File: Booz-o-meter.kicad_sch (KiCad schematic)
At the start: 61 parts, among them J1 Power, J4 Rod, K1 G5V-2, K2 G5V-2, K3 G5V-2, K4 G5V-2, K5 G5V-2, K6 G5V-2, K7 G5V-2, K8 G5V-2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

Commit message: First pass at routing
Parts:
- added H1, H2, H3, H4: MountingHole, MountingHole:MountingHole_3.5mm, symbol Mechanical:MountingHole
- added SW1, SW2: SW_MEC_5E, symbol Switch:SW_MEC_5E
- K1: value G5V-2 -> GAME_ACTIVE1
- K2: value G5V-2 -> GAME_OVER
- K3: value G5V-2 -> ZAPOSC
- K4: value G5V-2 -> GAME_ACTIVE2
- K5: value G5V-2 -> FWD
- K6: value G5V-2 -> LOST
- K7: value G5V-2 -> REV
- K8: value G5V-2 -> WON
- K9: value G5V-2 -> GAME_RESET
- SW_FWD_LIMIT1: symbol Switch:SW_SPDT -> Switch:SW_SPST
- renumbered RV1 to GAME_OVER_TIMER1
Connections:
- net GND: now also SW2.3 (K)
- net VCC: now also K1.1; no longer K1.16
- net game_active: now also K1.16; no longer K1.1
- net at D9.1 (KA), R4.2: now also PB_RESET1.3 (K)
- net at K1.8, K2.13, PB_START1.2: now also SW1.3 (K), SW1.4 (A)
- net at K1.9, K7.1, R10.1: now also D24.1 (K)
- net at D9.2 (AK), K5.13, K7.13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: now also PB_RESET1.4 (A)
- net at PB_START1.1, PB_START1.3 (K), SW_REV_LIMIT1.1 (A): now also SW1.1, SW1.2
- net at D15.1 (K), PB_RESET1.2: now also SW2.2
- no-connect marks 0 -> 3
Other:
- note removed: "**POWER CONNECTOR!!!**"
- note removed: "**VMOTOR**"
- note removed: "**VTRANS**"
- moved on the sheet: D11, D12, R2

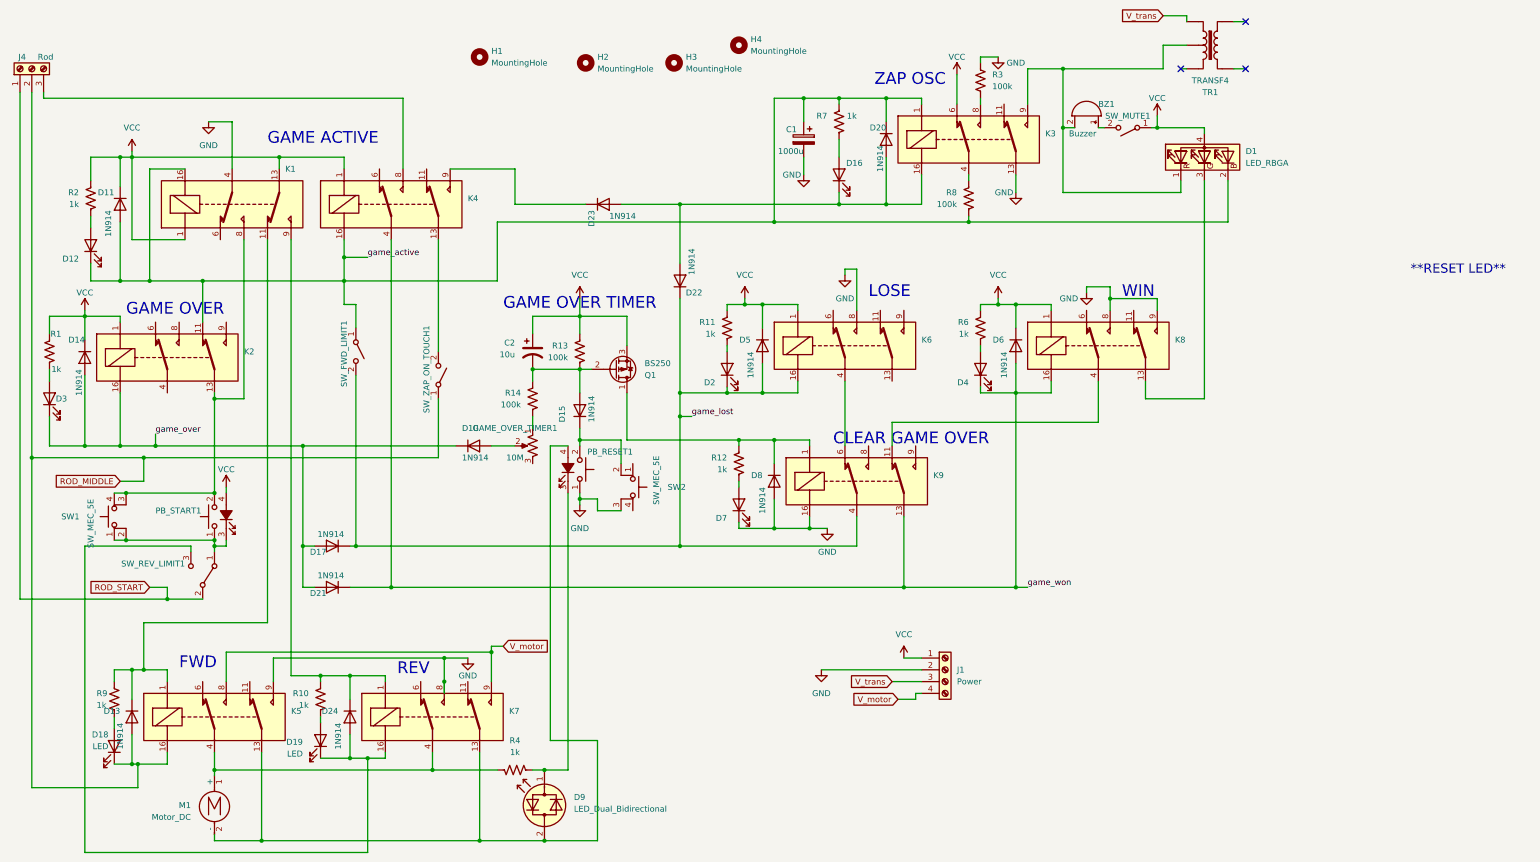
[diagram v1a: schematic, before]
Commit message: Fix zap on touch, add motor series R, clean DRC
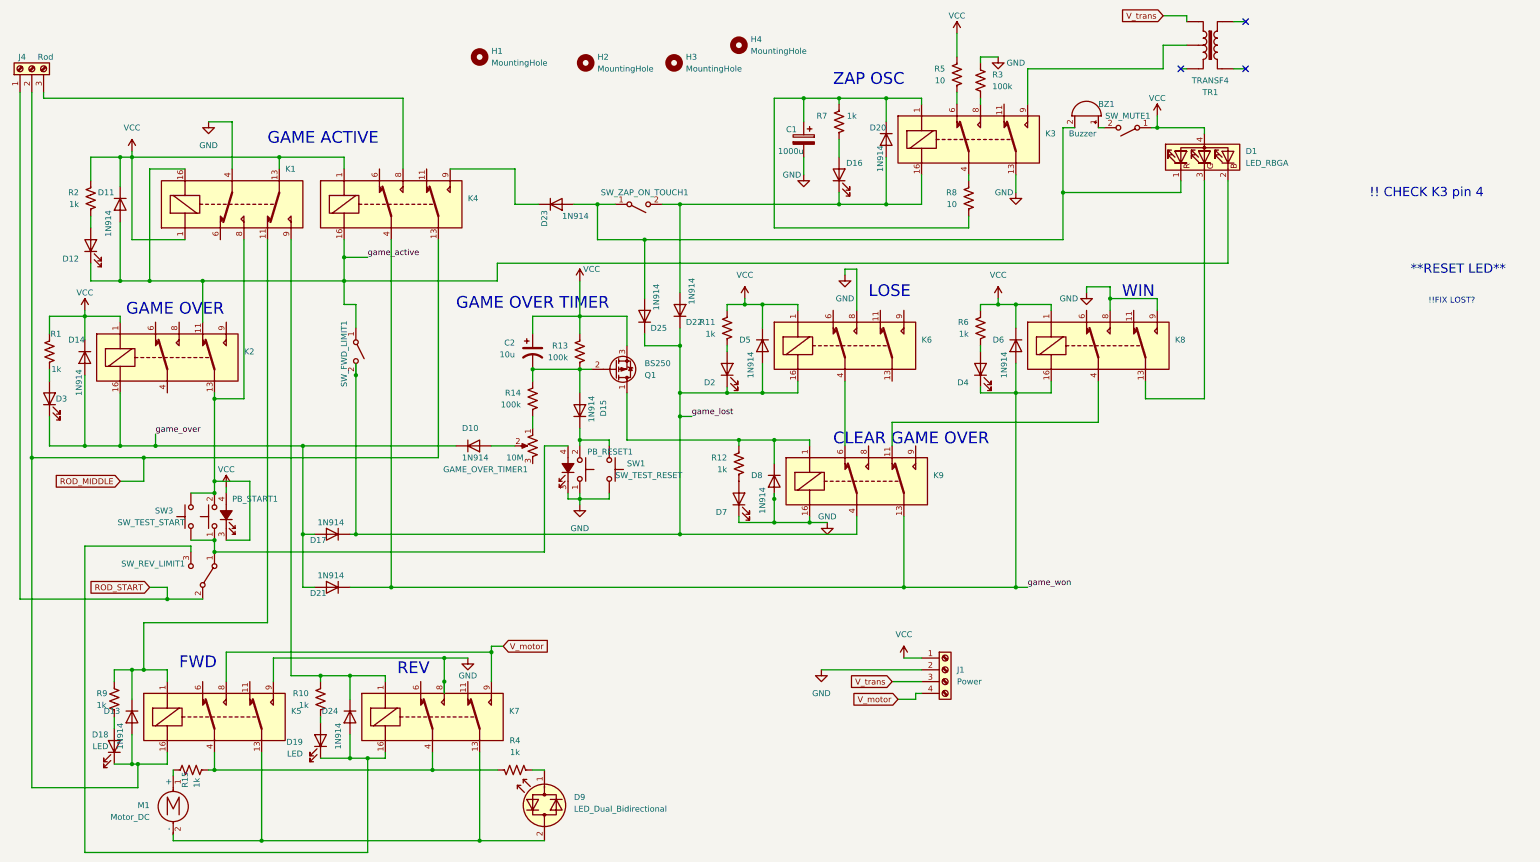
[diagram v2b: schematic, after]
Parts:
- removed SW1, SW2: SW_MEC_5E, symbol Switch:SW_MEC_5E
- added D25: 1N914, Diode_THT:D_DO-35_SOD27_P7.62mm_Horizontal, symbol Diode:1N914
- added R15: 1k, Resistor_THT:R_Axial_DIN0207_L6.3mm_D2.5mm_P10.16mm_Horizontal, symbol Device:R_US
- added R5: 10, Resistor_THT:R_Axial_DIN0204_L3.6mm_D1.6mm_P5.08mm_Horizontal, symbol Device:R_US
- added SW1: SW_TEST_RESET, Button_Switch_THT:SW_PUSH_6mm, symbol Switch:SW_Push
- added SW3: SW_TEST_START, Button_Switch_THT:SW_PUSH_6mm, symbol Switch:SW_Push
- R8: value 100k -> 10
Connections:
- net GND: now also PB_RESET1.3 (K), SW1.2
- net ROD_MIDDLE: now also K4.13; no longer SW_ZAP_ON_TOUCH1.1 (A)
- net VCC: now also R5.1; no longer K3.6
- net game_active: no longer C1.1, D20.1 (K), K3.1, R7.1, R8.2
- net game_lost: now also D25.1 (K)
- net at D15.1 (K), PB_RESET1.2: now also SW1.1
- net at D16.1 (K), D20.2 (A), D22.2 (A)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: now also SW_ZAP_ON_TOUCH1.2 (B); no longer D23.2 (A)
- net at K3.9, TR1.2: no longer BZ1.2 (+), D1.1 (RK)
- net at K5.4, K7.4, R4.1: now also R15.2; no longer M1.1 (+)
- net at D9.1 (KA), R4.2: no longer PB_RESET1.3 (K)
- net at K1.8, K2.13, PB_START1.2: now also PB_START1.3 (K), SW3.1
- net at D9.2 (AK), K5.13, K7.13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: no longer PB_RESET1.4 (A)
- net at PB_START1.1, SW_REV_LIMIT1.1 (A): now also PB_RESET1.4 (A), SW3.2; no longer PB_START1.3 (K)
- new net: C1.1, D20.1 (K), K3.1, R7.1, R8.2
- new net: K3.6, R5.2
- new net: BZ1.2 (+), D1.1 (RK), D23.2 (A), D25.2 (A), SW_ZAP_ON_TOUCH1.1 (A)
- new net: M1.1 (+), R15.1
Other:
- note added: "!! CHECK K3 pin 4"
- note added: "!!FIX LOST?"
- moved on the sheet: D17, D22, D23, D7, M1, SW_ZAP_ON_TOUCH1

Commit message: Increase resistor pitch to 0.4, add silk text
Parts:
- R1, R10, R11, R12, R13, R14, R2, R3, R4, R5, R6, R7, R8, R9: footprint Resistor_THT:R_Axial_DIN0204_L3.6mm_D1.6mm_P5.08mm_Horizontal -> Resistor_THT:R_Axial_DIN0207_L6.3mm_D2.5mm_P10.16mm_Horizontal
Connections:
- no-connect marks 3 -> 4
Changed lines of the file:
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@@
   )
   (no_connect (at 279.4 25.4))
+  (no_connect (at 125.73 113.03))
   (no_connect (at 279.4 15.24))
   (no_connect (at 265.43 25.4))
@@
       (effects (font (size 1.27 1.27)) (justify left))
     )
-    (property "Footprint" "Resistor_THT:R_Axial_DIN0204_L3.6mm_D1.6mm_P5.08mm_Horizontal" (at 218.694 53.594 90)
+    (property "Footprint" "Resistor_THT:R_Axial_DIN0207_L6.3mm_D2.5mm_P10.16mm_Horizontal" (at 218.694 53.594 90)
       (effects (font (size 1.27 1.27)) hide)
     )
@@
       (effects (font (size 1.27 1.27)) (justify left))
     )
-    (property "Footprint" "Resistor_THT:R_Axial_DIN0204_L3.6mm_D1.6mm_P5.08mm_Horizontal" (at 36.576 161.544 90)
+    (property "Footprint" "Resistor_THT:R_Axial_DIN0207_L6.3mm_D2.5mm_P10.16mm_Horizontal" (at 36.576 161.544 90)
       (effects (font (size 1.27 1.27)) hide)
     )
@@
       (effects (font (size 1.27 1.27)))
     )
-    (property "Footprint" "Resistor_THT:R_Axial_DIN0204_L3.6mm_D1.6mm_P5.08mm_Horizontal" (at 122.174 177.546 90)
+    (property "Footprint" "Resistor_THT:R_Axial_DIN0207_L6.3mm_D2.5mm_P10.16mm_Horizontal" (at 122.174 177.546 90)
       (effects (font (size 1.27 1.27)) hide)
     )
@@
       (effects (font (size 1.27 1.27)) (justify left))
     )
-    (property "Footprint" "Resistor_THT:R_Axial_DIN0204_L3.6mm_D1.6mm_P5.08mm_Horizontal" (at 216.154 26.924 90)
+    (property "Footprint" "Resistor_THT:R_Axial_DIN0207_L6.3mm_D2.5mm_P10.16mm_Horizontal" (at 216.154 26.924 90)
       (effects (font (size 1.27 1.27)) hide)
     )
@@
       (effects (font (size 1.27 1.27)) (justify left))
     )
-    (property "Footprint" "Resistor_THT:R_Axial_DIN0204_L3.6mm_D1.6mm_P5.08mm_Horizontal" (at 29.464 53.594 90)
+    (property "Footprint" "Resistor_THT:R_Axial_DIN0207_L6.3mm_D2.5mm_P10.16mm_Horizontal" (at 29.464 53.594 90)
       (effects (font (size 1.27 1.27)) hide)
     )
@@
       (effects (font (size 1.27 1.27)) (justify left))
     )
-    (property "Footprint" "Resistor_THT:R_Axial_DIN0204_L3.6mm_D1.6mm_P5.08mm_Horizontal" (at 169.164 110.744 90)
+    (property "Footprint" "Resistor_THT:R_Axial_DIN0207_L6.3mm_D2.5mm_P10.16mm_Horizontal" (at 169.164 110.744 90)
       (effects (font (size 1.27 1.27)) hide)
     )
@@
       (effects (font (size 1.27 1.27)) (justify left))
     )
-    (property "Footprint" "Resistor_THT:R_Axial_DIN0204_L3.6mm_D1.6mm_P5.08mm_Horizontal" (at 20.574 86.614 90)
+    (property "Footprint" "Resistor_THT:R_Axial_DIN0207_L6.3mm_D2.5mm_P10.16mm_Horizontal" (at 20.574 86.614 90)
       (effects (font (size 1.27 1.27)) hide)
     )
@@
       (effects (font (size 1.27 1.27)) (justify left))
     )
-    (property "Footprint" "Resistor_THT:R_Axial_DIN0204_L3.6mm_D1.6mm_P5.08mm_Horizontal" (at 78.994 161.544 90)
+    (property "Footprint" "Resistor_THT:R_Axial_DIN0207_L6.3mm_D2.5mm_P10.16mm_Horizontal" (at 78.994 161.544 90)
       (effects (font (size 1.27 1.27)) hide)
     )
@@
       (effects (font (size 1.27 1.27)) (justify left))
     )
-    (property "Footprint" "Resistor_THT:R_Axial_DIN0204_L3.6mm_D1.6mm_P5.08mm_Horizontal" (at 124.714 96.774 90)
+    (property "Footprint" "Resistor_THT:R_Axial_DIN0207_L6.3mm_D2.5mm_P10.16mm_Horizontal" (at 124.714 96.774 90)
       (effects (font (size 1.27 1.27)) hide)
     )
@@
       (effects (font (size 1.27 1.27)) (justify left))
     )
-    (property "Footprint" "Resistor_THT:R_Axial_DIN0204_L3.6mm_D1.6mm_P5.08mm_Horizontal" (at 134.874 86.614 90)
+    (property "Footprint" "Resistor_THT:R_Axial_DIN0207_L6.3mm_D2.5mm_P10.16mm_Horizontal" (at 134.874 86.614 90)
       (effects (font (size 1.27 1.27)) hide)
     )
@@
       (effects (font (size 1.27 1.27)) (justify left))
     )
-    (property "Footprint" "Resistor_THT:R_Axial_DIN0204_L3.6mm_D1.6mm_P5.08mm_Horizontal" (at 223.266 28.194 90)
+    (property "Footprint" "Resistor_THT:R_Axial_DIN0207_L6.3mm_D2.5mm_P10.16mm_Horizontal" (at 223.266 28.194 90)
       (effects (font (size 1.27 1.27)) hide)
     )
@@
       (effects (font (size 1.27 1.27)) (justify left))
     )
-    (property "Footprint" "Resistor_THT:R_Axial_DIN0204_L3.6mm_D1.6mm_P5.08mm_Horizontal" (at 221.234 81.534 90)
+    (property "Footprint" "Resistor_THT:R_Axial_DIN0207_L6.3mm_D2.5mm_P10.16mm_Horizontal" (at 221.234 81.534 90)
       (effects (font (size 1.27 1.27)) hide)
     )
@@
       (effects (font (size 1.27 1.27)) (justify left))
     )
-    (property "Footprint" "Resistor_THT:R_Axial_DIN0204_L3.6mm_D1.6mm_P5.08mm_Horizontal" (at 166.624 81.534 90)
+    (property "Footprint" "Resistor_THT:R_Axial_DIN0207_L6.3mm_D2.5mm_P10.16mm_Horizontal" (at 166.624 81.534 90)
       (effects (font (size 1.27 1.27)) hide)
     )
@@
       (effects (font (size 1.27 1.27)) (justify left))
     )
-    (property "Footprint" "Resistor_THT:R_Axial_DIN0204_L3.6mm_D1.6mm_P5.08mm_Horizontal" (at 190.754 37.084 90)
+    (property "Footprint" "Resistor_THT:R_Axial_DIN0207_L6.3mm_D2.5mm_P10.16mm_Horizontal" (at 190.754 37.084 90)
       (effects (font (size 1.27 1.27)) hide)
     )

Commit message: Final tweaks before send out
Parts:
- added D26: 1N914, Diode_THT:D_DO-35_SOD27_P7.62mm_Horizontal, symbol Diode:1N914
- D1: value LED_RBGA -> LED_RGBA; symbol Device:LED_RBGA -> Device:LED_RGBA
- K1: value GAME_ACTIVE1 -> G5V-2
- K2: value GAME_OVER -> G5V-2
- K3: value ZAPOSC -> G5V-2
- K4: value GAME_ACTIVE2 -> G5V-2
- K5: value FWD -> G5V-2
- K6: value LOST -> G5V-2
- K7: value REV -> G5V-2
- K8: value WON -> G5V-2
- K9: value GAME_RESET -> G5V-2
- R15: value 1k -> 5
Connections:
- net game_active: now also D1.3 (BK); no longer D1.2 (BK)
- net game_over: now also D26.1 (K)
- net at D13.1 (K), K5.1, R9.1: now also K1.9; no longer K1.11
- net ROD_WIN: now reaches J4.3 (Pin_3), K4.8
- net at D24.1 (K), K7.1, R10.1: now also K1.11; no longer K1.9
- net at K8.13: now also D1.2 (GK); no longer D1.3 (GK)
- net at D15.1 (K), PB_RESET1.2, SW1.1: now also D26.2 (A)
- no-connect marks 4 -> 24
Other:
- note removed: "!! CHECK K3 pin 4"
- note removed: "!!FIX LOST?"
- note removed: "**RESET LED**"
- moved on the sheet: D10, J1, R14
